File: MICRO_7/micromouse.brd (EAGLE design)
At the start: 96 x 72 mm, 34 parts

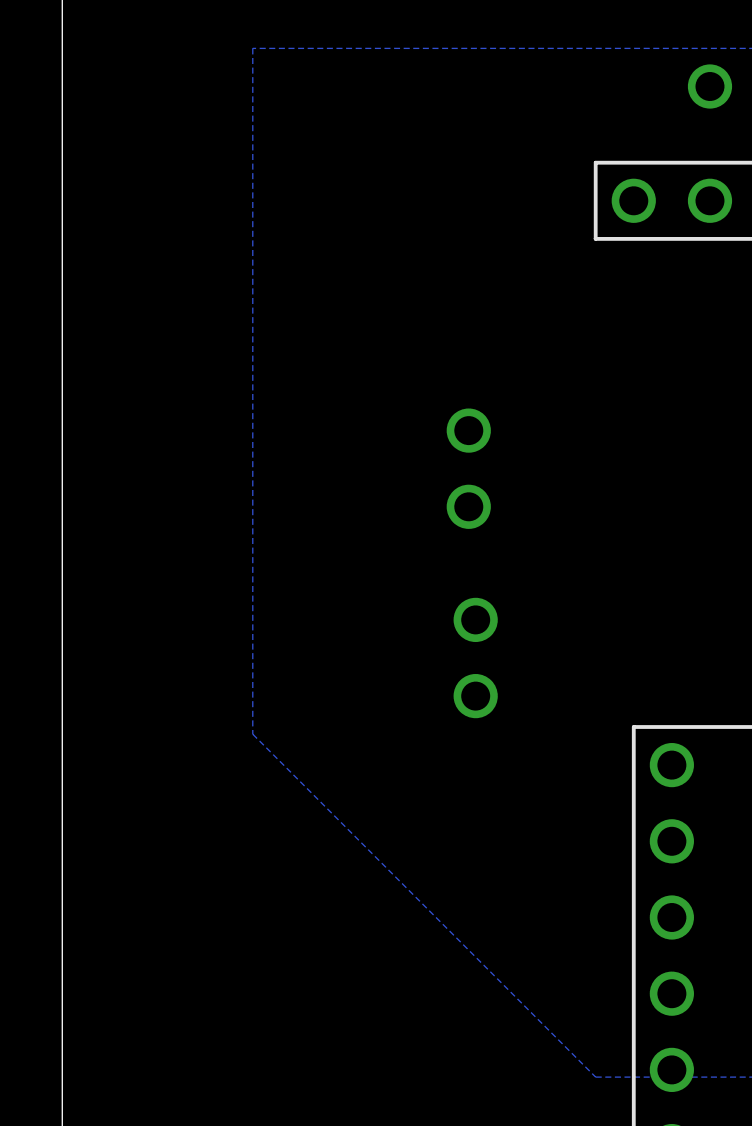
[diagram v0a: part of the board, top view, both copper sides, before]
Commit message: added back place for ball caster
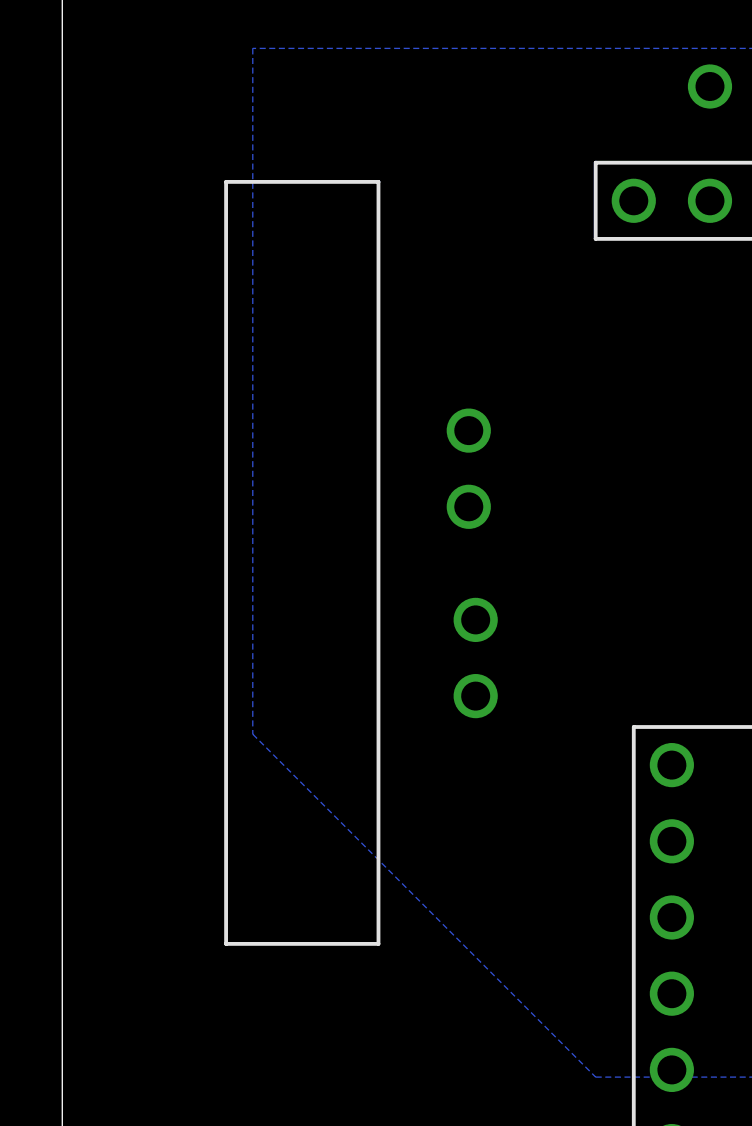
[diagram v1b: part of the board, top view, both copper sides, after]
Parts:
- added U$21: BALL_CASTER, BALL_CASTER:BALL_CASTER
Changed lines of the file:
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@@
 <element name="U$19" library="MOTOR_BRACKET" package="MOTOR_BRACKET" value="MOTOR_BRACKET" x="47" y="68.38"/>
 <element name="U$20" library="BALL_CASTER" package="BALL_CASTER" value="BALL_CASTER" x="72" y="40" rot="R270"/>
+<element name="U$21" library="BALL_CASTER" package="BALL_CASTER" value="BALL_CASTER" x="8" y="40" rot="R90"/>
 </elements>
 <signals>

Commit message: traced all of the connections
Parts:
- moved U$4 26.7 mm to (25.4, 40.1), turned to 0 degrees
- moved U$2 24.6 mm to (43.7, 39.9), turned to 90 degrees
- moved U$3 23.0 mm to (25.3, 39.9), turned to 0 degrees
- moved U$1 22.6 mm to (48.8, 40.1), turned to 270 degrees
- moved U$11 21.2 mm to (7.86, 70.9)
- moved U$10 20.5 mm to (6.59, 66.1)
- moved U$13 10.9 mm to (26.8, 18.6), turned to 270 degrees
- moved R10 2.00 mm to (74.9, 54.1)
- moved R6 2.00 mm to (61.7, 24.7)
- moved R9 2.00 mm to (74.9, 58.2)
- moved R5 1.00 mm to (61.7, 28.8)
- moved U$5 1.00 mm to (63.1, 61.6)
- moved U$7 1.00 mm to (68.6, 17.6)
- moved U$8 1.00 mm to (62.9, 18.1)
- moved U$9 1.00 mm to (68.9, 62.4)
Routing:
- net 3.3V_VCC: track 0.00 -> 178.7 mm, vias 0 -> 2
- net N$13: track 0.00 -> 119.1 mm
- net N$25: track 0.00 -> 107.1 mm, vias 0 -> 2
- net N$14: track 0.00 -> 106.6 mm, vias 0 -> 8
- net 5V_VCC: track 0.00 -> 99.3 mm
- net OUTA_L: track 0.00 -> 92.6 mm, vias 0 -> 4
- net N$9: track 0.00 -> 87.5 mm, vias 0 -> 3
- net N$11: track 0.00 -> 82.4 mm, vias 0 -> 10
- net M2_L: track 0.00 -> 81.6 mm
- net N$8: track 0.00 -> 79.4 mm, vias 0 -> 8
- net N$6: track 0.00 -> 79.3 mm, vias 0 -> 8
- net N$2: track 0.00 -> 73.1 mm, vias 0 -> 3
- net N$22: track 0.00 -> 68.0 mm, vias 0 -> 4
- net OUTB_L: track 0.00 -> 64.3 mm, vias 0 -> 6
- net M1_L: track 0.00 -> 64.3 mm
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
